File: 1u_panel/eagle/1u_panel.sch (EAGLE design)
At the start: 100 parts, among them J1 SAMTEC-MMS-104-02-X-SHJ, J2 ORESAT-DEBUG-CONNECTOR-SOLAR, Q1 MOSFET-PCH-SOT23-6, Q2 MOSFET-PCH-SOT23-6, U1 TCAN330, U10 TPS63070, U11 TMP101NA/3KSLOTTED, U12 LTC4412, U2 TMP101NA/3KSLOTTED, U3 LT1618EMSTRPBF, U4 INA226AIDGSR, U7 STM32F091C, X2 16MHZ-2.5x2mm

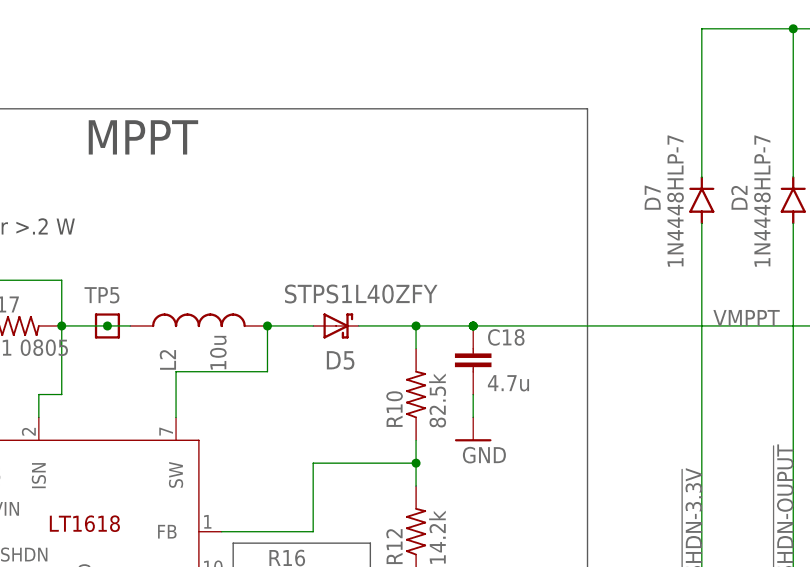
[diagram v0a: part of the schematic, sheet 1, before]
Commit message: updated attributes and BOM
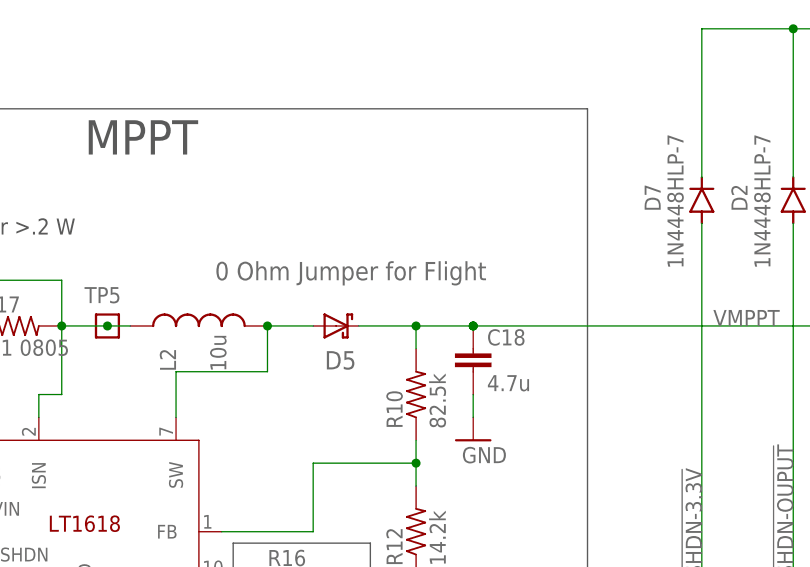
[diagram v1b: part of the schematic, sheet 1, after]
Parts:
- D5: value STPS1L40ZFY -> 0 Ohm Jumper for Flight
- J2: DIS (none) -> Digi-Key; DPN (none) -> 732-11341-1-ND; MFR (none) -> Wurth; MPN (none) -> 687120183622
- L2: DIS (none) -> Digi-Key; DPN (none) -> 732-1025-1-ND
- Q1: DIS (none) -> Digi-Key; DPN (none) -> DMP2240UDMDICT-ND; MFR (none) -> Diodes Inc.; MPN (none) -> DMP2240UDM-7
- Q2: DIS (none) -> Digi-Key; DPN (none) -> DMP3050LVT-7DICT-ND; MFR (none) -> Diodes Inc.; MPN (none) -> DMP3050LVT-7
- R16: DIS (none) -> Digi-Key; DPN (none) -> 2019-RK73H1JTTD2001FCT-ND; MFR (none) -> KOA; MPN (none) -> RK73H1JTTD2001F
- U10: DIS (none) -> Digi-Key; DPN (none) -> 296-44764-1-ND; MFR (none) -> Texas Instruments; MPN (none) -> TPS63070RNMT
- U11, U2: DIS (none) -> Digi-Key; DPN (none) -> 296-27725-1-ND; MFR (none) -> Texas Instruments; MPN (none) -> TMP101NA/3K
- U12: DIS (none) -> Digi-Key; DPN (none) -> LTC4412ES6#TRPBFCT-ND; MFR (none) -> Linear Technologies; MPN (none) -> LTC4412ES6#TRPBF
- U3: DIS (none) -> Digi-Key; DPN (none) -> LT1618EMS#TRPBFCT-ND; MFR (none) -> Linear Technologies; MPN (none) -> LT1618EMS#TRPBF
- U4: DIS (none) -> Digi-Key; DPN (none) -> 296-29034-1-ND
- U7: DPN 497-18516-ND -> 497-18749-1-ND; MPN STM32F042K6T7 -> STM32F091CCT6TR

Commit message: UUuugggghhhh merged David's changes, NOW everything is nicely cleaned up with his attributes.
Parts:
- removed CF2: J-HARWIN-M55-6021242R, J-Harwin-M55-6021242R:J-HARWIN-M55-6021242R
- added CF1: HARWIN M55-6021242R, J-Harwin-M55-60X1242R-Solar-board-connector:SOLAR-BOARD-CONNECTOR
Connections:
- removed net !SHUTDOWN: CF2.1, CF2.2, D2.C, D7.C, J1.2A, J1.2B, J1.4A, J1.4B, TP11.1
- new net !SD: CF1.!SD, D2.C, D7.C, J1.2A, J1.2B, J1.4A, J1.4B, TP11.1
- net AUX: now also CF1.AUX; no longer CF2.7, CF2.8
- net CANH: now also CF1.CANH; no longer CF2.10, CF2.9
- net CANL: now also CF1.CANL; no longer CF2.11, CF2.12
- net GND: now also CF1.GND, CF1.SHIELD; no longer CF2.3, CF2.4, CF2.SHIELDS
- net VBUS: now also CF1.VBUS; no longer CF2.5, CF2.6
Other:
- note added: "5"
- note added: "OreSat Solar Board: MPPT + PWR"
- note added: "OreSat Solar Board: Microcontroller"
- note removed: "3"
- note removed: "OreSat Solar Module"
- moved on the sheet: C21, J1, Q1, Q2.1, Q2.2, R19, TP1, TP12, TP14, TP16, U12

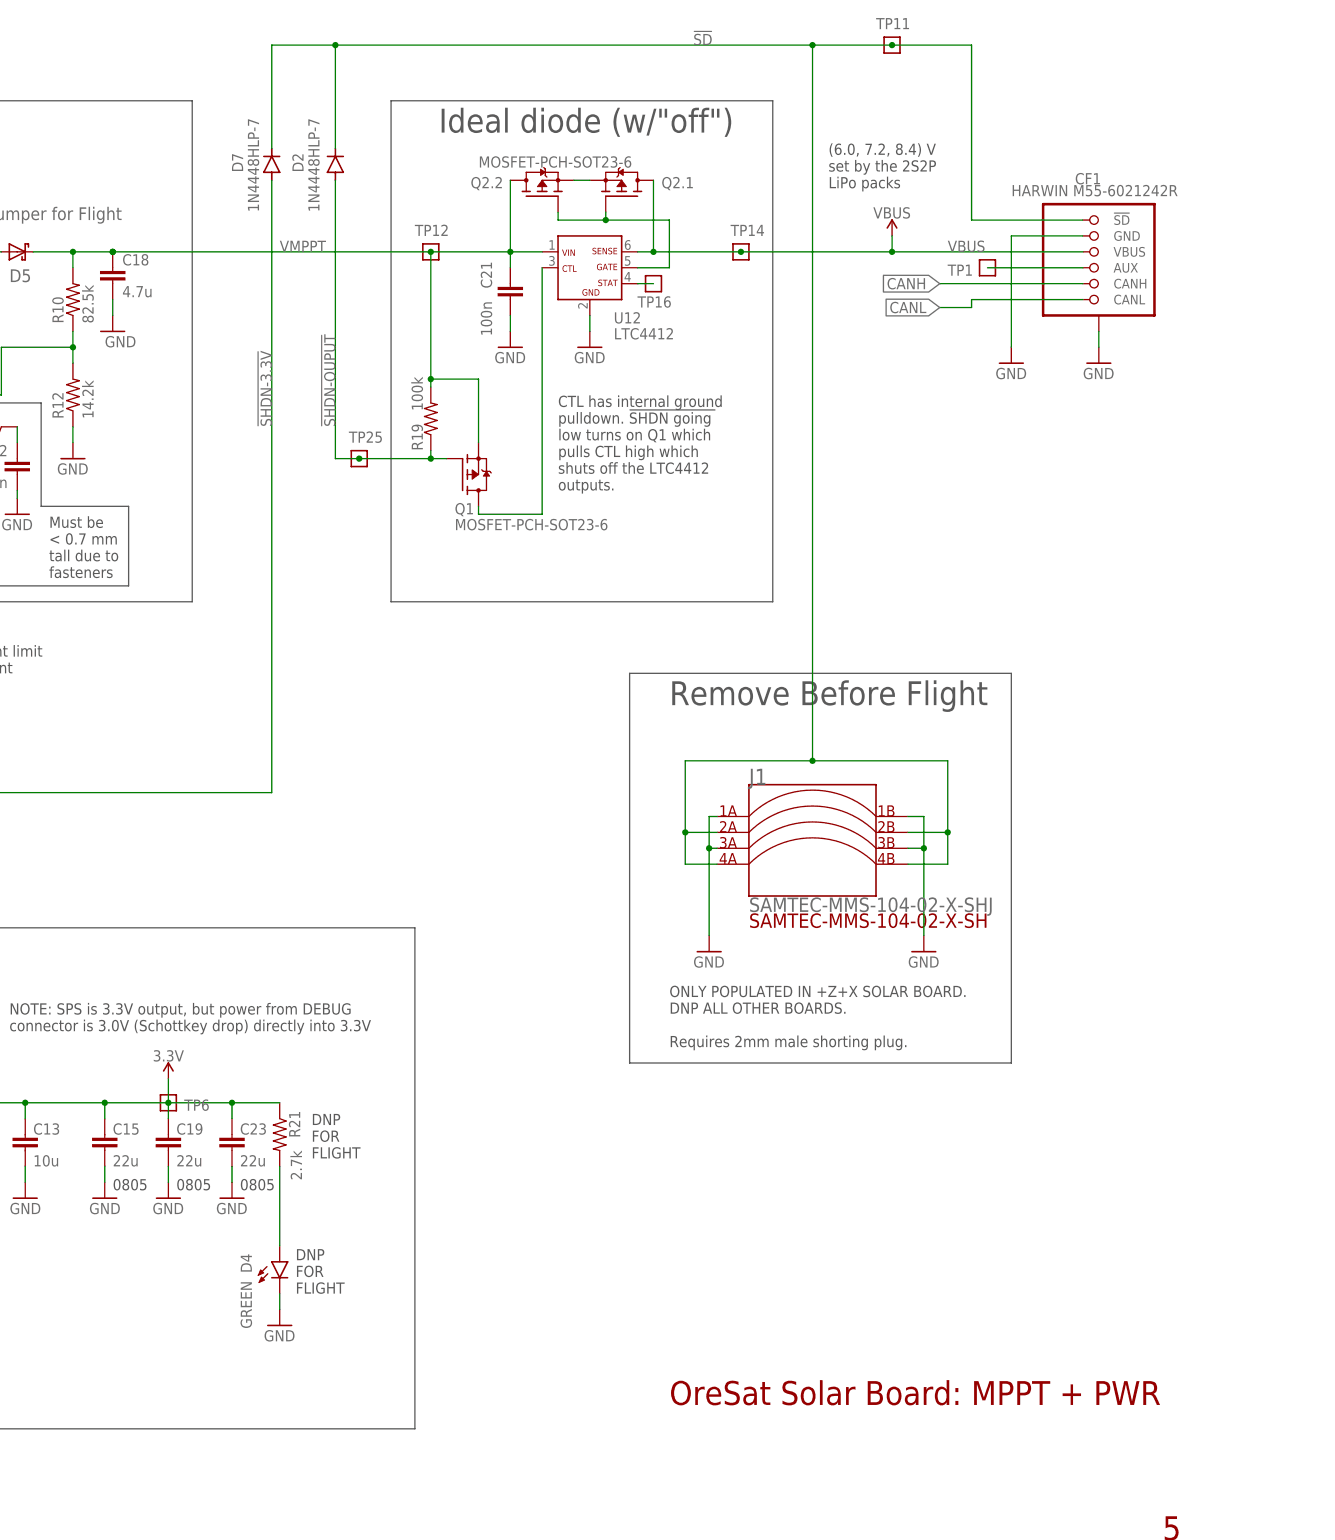
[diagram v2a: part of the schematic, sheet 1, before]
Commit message: Fixed bizarre inconsistancy error?
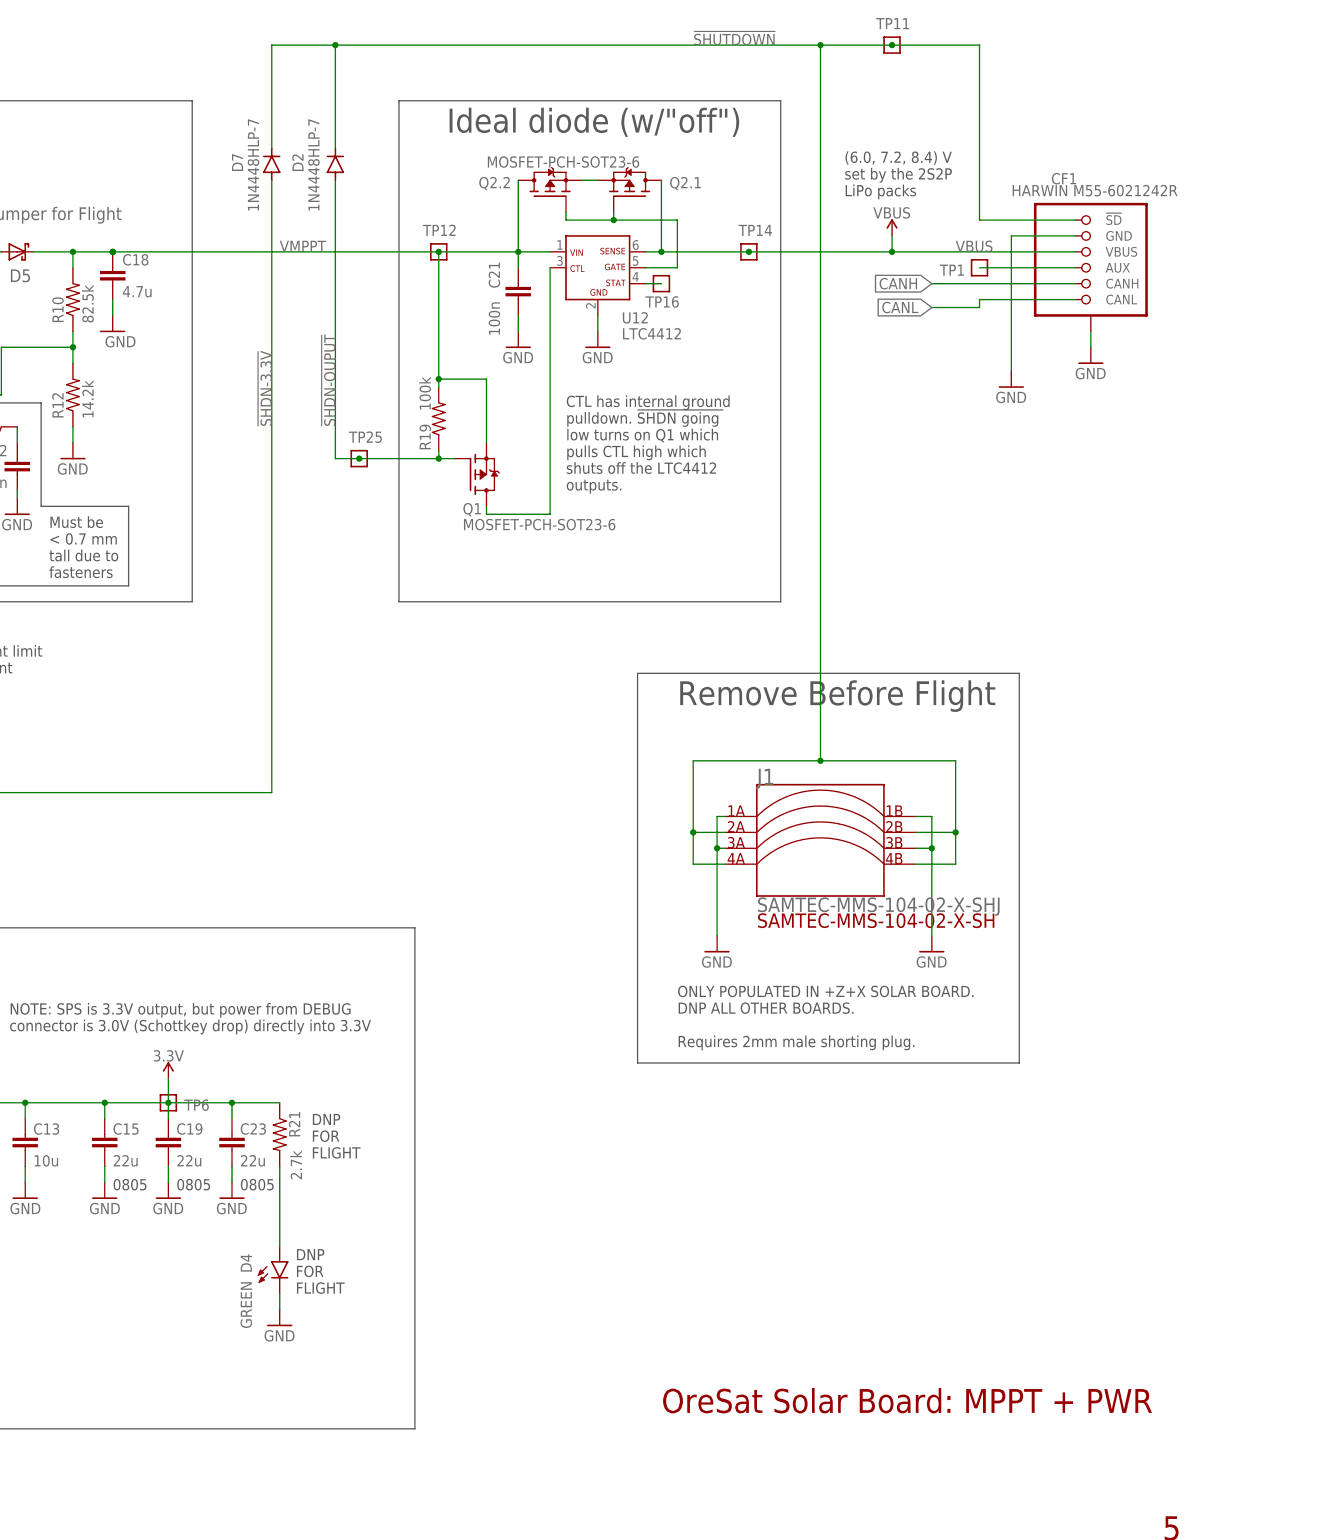
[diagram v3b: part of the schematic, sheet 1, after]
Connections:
- net !SD renamed !SHUTDOWN
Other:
- moved on the sheet: C21, CF1, J1, Q1, Q2.1, Q2.2, R19, TP1, TP12, TP14, TP16, U12

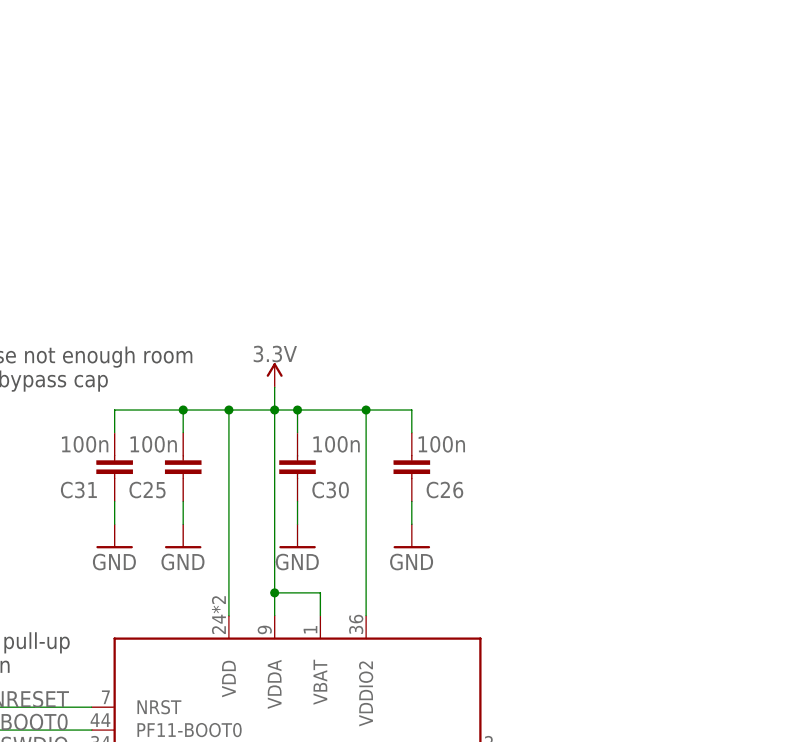
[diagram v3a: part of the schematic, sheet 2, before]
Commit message: Added capacitor bank circuit for MCU and updated BOM
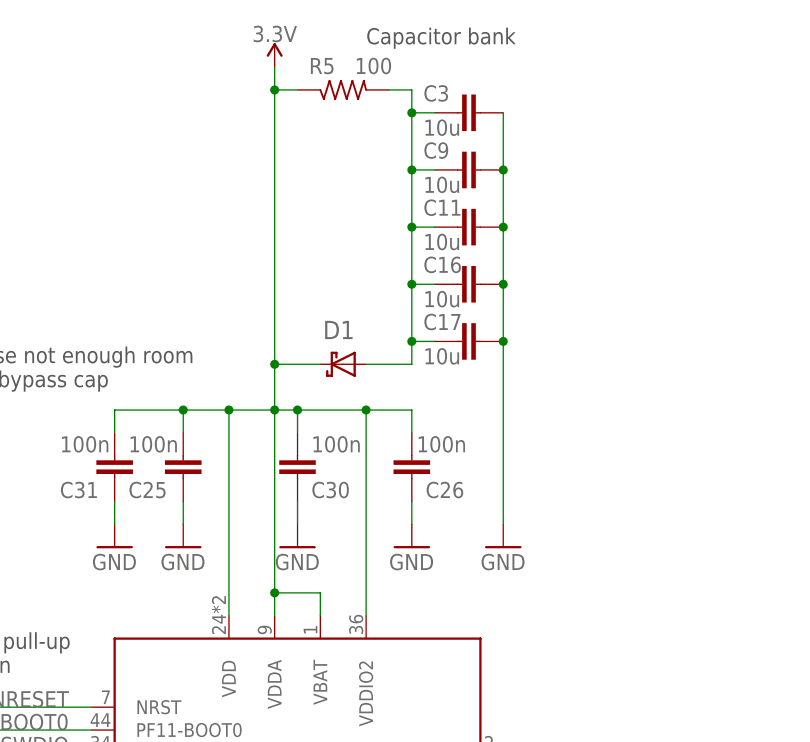
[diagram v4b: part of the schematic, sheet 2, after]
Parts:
- added C11, C16, C17, C3, C9: 10u, oresat-rcl:C-EU0805-B-NOSILK
- added D1: DIODE-SCHOTTKY-MBR0520L, apdm-ic-v2:DIODE-SCHOTTKY-MBR0520L
- added R5: 100, oresat-rcl:R-US_0805-C-NOSILK
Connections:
- new net N$3: C11.1, C16.1, C17.1, C3.1, C9.1, D1.ANODE, R5.2
- net 3.3V: now also D1.CATHODE, R5.1
- net GND: now also C11.2, C16.2, C17.2, C3.2, C9.2
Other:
- note added: "Capacitor bank"

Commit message: solar V5.1
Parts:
- added U$2: FLIGHMARKEROLD, oresat-flight-marker:FLIGHMARKEROLD
- L2: device L-Bourns-SRN4018TA:L-BOURNS-SRN4018TA -> Wurth-744042100:L-WURTH-744042100
- R11, R9: DIS Digi-Key -> (none); DPN 1276-4275-1-ND -> (none); MFR Samsung -> (none); MPN RC1005F6653CS -> (none)
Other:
- note added: "5.1"

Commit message: tweaks to solar V5.1
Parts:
- added R20: 0, oresat-rcl:R-US_0805-C-NOSILK
- added R24, R25, R26, R27: 1k, oresat-rcl:R-US_0603-C-NOSILK
- C11, C16, C17, C3, C9: value 10u -> 22u
- L1: device L-Coilcraft-XFL4020:L-COILCRAFT-XFL4020 -> L-TDK-VLS3010CX-1R5M-1:VLS3010CX-1R5M-1; DIS Mouser -> Digi-Key; DPN 994-XFL4020-152MEB -> 445-VLS3010CX-1R5M-1CT-ND; MFR Coilcraft -> TDK; MPN XFL4020-152ME -> VLS3010CX-1R5M-1
- R3, R4: value 2.7k -> 4.7k; DIS Digi-Key -> (none); DPN A129693CT-ND -> (none); MFR TE -> (none); MPN CRGCQ0603F2K7 -> (none)
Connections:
- new net N$12: R27.1, U7.PB15
- new net N$4: C13.1, C15.1, C19.1, C23.1, R1.2, R20.2, R9.2, TP6.1, U10.VOUT
- new net N$5: R24.1, U7.PB12
- new net N$6: R25.1, U7.PB13
- new net N$8: R26.1, U7.PB14
- net 3.3V: now also R20.1; no longer C13.1, C15.1, C19.1, C23.1, R1.2, R9.2, TP6.1, U10.VOUT
- net GND: now also R24.2, R25.2, R26.2, R27.2
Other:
- note added: "NOTE: VBAT not bypassed becase not enough room instead tied into nearest bypass cap"
- note removed: "VBAT not bypassed becase not enough room instead tied into nearest bypass cap"
- moved on the sheet: D4, R21

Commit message: Silly OCD cleanup, nothing important.
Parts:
- removed U$2: FLIGHMARKEROLD, oresat-flight-marker:FLIGHMARKEROLD
- removed X2: 16MHZ-2.5x2mm, low-gain-radio:CRYSTAL-WITH-GND
- added U$1: FLIGHTMARKERNEW, oresat-flight-marker:FLIGHTMARKERNEW
- added X1: 16MHZ-2.5x2mm, low-gain-radio:CRYSTAL-WITH-GND
- R24, R25, R26, R27: value 1k -> 1k/NP
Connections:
- net N$12 renamed SMSN3
- net N$4 renamed TPS-VOUT-3.3V
- net N$5 renamed SMSN0
- net N$6 renamed SMSN1
- net N$8 renamed SMSN2
- removed net CRYSTALIN1: C28.1, U7.PF0-OSC_IN, X2.1
- removed net CRYSTALOUT1: C27.1, U7.PF1-OSC_OUT, X2.2
- new net XTAL1-IN: C28.1, U7.PF0-OSC_IN, X1.1
- new net XTAL1-OUT: C27.1, U7.PF1-OSC_OUT, X1.2
- net GND: now also X1.SHIELD; no longer X2.SHIELD
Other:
- note added: "RATE FOR > 200 mW"
- note added: "Solar module Serial Number Required by CAN messages. 0: +X+Z 1: -Y+Z 2: -X+Z 3: -Y+Z 4: +X-Z .. and so on."
- note removed: "NOTE: R5 should be rated for >.2 W"
- moved on the sheet: C27, C28, R22, R24, R25, R26, R27, TP13, TP7

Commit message: fixed tcream for debug and updated bom
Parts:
- C1, C25, C26, C29, C30, C31, C5, C6, C7, C8: DPN 399-14941-1-ND -> 1276-6985-1-ND; MPN C0603C104K4PAC7867 -> CL10B104KB85PND
- C10, C12: DPN 490-6473-1-ND -> 490-12379-2-ND; MPN GRM21BR61C106KE15K -> GRT21BR61C106KE01L
- C11, C16, C17, C3, C9: DPN 490-6473-1-ND -> 1276-6817-1-ND; MFR Murata -> Samsung; MPN GRM21BR61C106KE15K -> CL32B226KOJVPNE
- C13, C20, C4: DPN 490-12736-1-ND -> 490-12317-1-ND; MPN GRM188R61C106KAALJ -> GRT188R61C106KE13D
- C14, C18: DPN 490-10481-1-ND -> 587-4332-1-ND; MFR Murata -> Taiyo; MPN GRM188R61C475KAAJD -> EMK107BBJ475KAHT
- C15, C19, C23: DPN 1276-6526-1-ND -> 1276-6817-1-ND; MPN CL21A226KOQNNNE -> CL32B226KOJVPNE
- C2: DPN 478-0603YD103KAT2ACT-ND -> 587-5957-1-ND; MFR AVX -> Taiyo; MPN 0603YD103KAT2A -> UMK107B7103KAHT
- C21: DPN 399-1038-1-ND -> 1276-6985-1-ND; MPN C0402C103K4RACTU -> CL10B104KB85PND
- C27, C28: DPN 399-14498-1-ND -> 490-11157-2-ND; MFR Kemet -> Murata; MPN C0603C200K4GAC7867 -> GCM1885C2A200JA16D
- D1: value DIODE-SCHOTTKY-MBR0520L -> NRVB130TGSOD123; device apdm-ic-v2:DIODE-SCHOTTKY-MBR0520L -> D-OnSemi-NRVB130T3G:NRVB130TGSOD123
- D5: value 0 Ohm Jumper for Flight -> NRVB130TGSOD123; device apdm-ic-v2:DIODE-SCHOTTKY-MBR0520L -> D-OnSemi-NRVB130T3G:NRVB130TGSOD123; DIS (none) -> Digi-Key; DPN (none) -> NRVB130T3GOSCT-ND; MFR (none) -> OnSemi; MPN (none) -> NRVB130T3G
- J2: value ORESAT-DEBUG-CONNECTOR-SOLAR -> ORESAT-DEBUG-CONNECTOR-ALL; device oresat-debug-connector:ORESAT-DEBUG-CONNECTOR-SOLAR -> oresat-debug-connector:ORESAT-DEBUG-CONNECTOR-ALL
- R24, R25, R26, R27: DIS (none) -> Digi-Key; DPN (none) -> 118-CR0603AFX-1001ELFCT-ND; MFR (none) -> Bourns; MPN (none) -> CR0603AFX-1001ELF
- R3, R4: DIS (none) -> Digi-Key; DPN (none) -> 13-RE0603FRE074K7LCT-ND; MFR (none) -> Yageo; MPN (none) -> RE0603FRE074K7L
- U$1: value FLIGHTMARKERNEW -> FLIGHMARKEROLD; device oresat-flight-marker:FLIGHTMARKERNEW -> oresat-flight-marker:FLIGHMARKEROLD
